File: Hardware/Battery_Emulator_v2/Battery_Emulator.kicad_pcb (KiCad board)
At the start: 2 copper layers, 34.6 x 90.6 mm, 51 parts, among them J1 Vin, J2 USB4105-GF-A-060, J3 Cell1_Vout, Q1 IRFB7545PBF, SW1 Jumper, SW2 Jumper, U1 MCP4651T-103E_ST, U10 ATmega328PB-A, U2 ISO1640BDR, U3 74AHC2G125DP,125, U4 FT230XS-R, U5 KA78M05_TO252, U7 LM317_TO-220, U8 MCP6001UT-I/OT, U9 KA78M05_TO252, Y1 Crystal_GND24

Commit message: Update Battery_Emulator.kicad_pcb
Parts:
- removed RV3, RV4: R_POT, Connector_PinHeader_2.54mm:PinHeader_1x03_P2.54mm_Vertical
- removed SW1, SW2: Jumper, Jumper:SolderJumper-3_P1.3mm_Open_Pad1.0x1.5mm
- added C23: 100n, Capacitor_SMD:C_0805_2012Metric, F.Cu at (192.9, 92.6)
- added C24: 100n, Capacitor_SMD:C_0805_2012Metric, F.Cu at (146.6, 87.4)
- added C25: 10u, Capacitor_SMD:C_0805_2012Metric, F.Cu at (129.4, 87.3)
- added C26: 100n, Capacitor_SMD:C_0805_2012Metric, F.Cu at (192.9, 101.6)
- added C27: 100n, Capacitor_SMD:C_0805_2012Metric, F.Cu at (192.9, 104.6)
- added C28: 10u, Capacitor_SMD:C_0805_2012Metric, F.Cu at (129.0, 92.4)
- added C29: 100n, Capacitor_SMD:C_0805_2012Metric, F.Cu at (146.6, 91.5)
- added C30: 100n, Capacitor_SMD:C_0805_2012Metric, F.Cu at (197.4, 95.6)
- added C31: 100n, Capacitor_SMD:C_0805_2012Metric, F.Cu at (197.4, 98.6)
- added C32: 100n, Capacitor_SMD:C_0805_2012Metric, F.Cu at (145.8, 94.3)
- added C33: 100n, Capacitor_SMD:C_0805_2012Metric, F.Cu at (197.4, 104.6)
- added J4: Cell1_Vout, TerminalBlock_Phoenix:TerminalBlock_Phoenix_MKDS-1,5-2-5.08_1x02_P5.08mm_Horizontal, F.Cu at (155.6, 143.2)
- added JP4: Jumper, Jumper:SolderJumper-3_P1.3mm_Open_Pad1.0x1.5mm_NumberLabels, F.Cu at (190.4, 114.9)
- added JP5: Jumper, Jumper:SolderJumper-3_P1.3mm_Open_Pad1.0x1.5mm_NumberLabels, F.Cu at (150.0, 94.0)
- added JP6: Jumper, Jumper:SolderJumper-3_P1.3mm_Open_Pad1.0x1.5mm_NumberLabels, F.Cu at (150.0, 90.7)
- added PS2: MEE1S1209SC, Converter_DCDC:Converter_DCDC_Murata_MEE1SxxxxSC_THT, F.Cu at (132.0, 85.7)
- added Q2: IRFB7545PBF, Package_TO_SOT_THT:TO-220-3_Horizontal_TabUp, F.Cu at (151.5, 129.6)
- added R10: 0.5m, Resistor_SMD:R_2512_6332Metric, F.Cu at (197.5, 122.1)
- added R8: 780k, Resistor_SMD:R_0805_2012Metric, F.Cu at (154.1, 90.7)
- added R9: 47, Resistor_SMD:R_0805_2012Metric, F.Cu at (201.8, 95.5)
- added U11: ISO1640BDR, Package_SO:SO-8_3.9x4.9mm_P1.27mm, F.Cu at (142.7, 89.4)
- added U12: MCP4651T-103E_ST, Package_SO:TSSOP-14_4.4x5mm_P0.65mm, F.Cu at (197.6, 116.4)
- added U13: KA78M05_TO252, Package_TO_SOT_SMD:TO-252-2, F.Cu at (182.3, 117.1)
- added U14: MCP6001UT-I/OT, Package_TO_SOT_SMD:SOT-23-5, F.Cu at (190.1, 126.0)
- added U6: LM317_TO-220, Package_TO_SOT_THT:TO-220-3_Horizontal_TabUp, F.Cu at (151.6, 114.1)
- R1: value 390k -> 780k
- moved Q1 55.5 mm to (117.6, 134.7)
- moved J3 55.5 mm to (123.5, 143.2)
- moved C1 55.4 mm to (120.0, 106.0)
- moved C11 55.4 mm to (109.2, 66.3)
- moved C12 55.4 mm to (111.2, 83.2)
- moved C15 55.4 mm to (117.6, 91.4)
- moved C16 55.4 mm to (99.9, 92.3)
- moved C17 55.4 mm to (100.1, 87.2)
- moved C18 55.4 mm to (117.6, 87.4)
- moved C2 55.4 mm to (120.0, 102.5)
- moved C21 55.4 mm to (122.6, 68.1)
- moved C22 55.4 mm to (109.2, 62.9)
- moved C3 55.4 mm to (116.6, 121.4)
- moved C4 55.4 mm to (122.7, 56.7)
- moved C5 55.4 mm to (125.4, 60.2)
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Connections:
- C3 pad 1: Net-(SW2-B) -> Net-(U1-P1W)
- U1 pad 6: Net-(SW2-C) -> Net-(U1-P1W)
- U1 pad 9: Net-(SW1-C) -> Net-(U1-P0W)
- U7 pad 1: Net-(SW2-B) -> Net-(U1-P1W)
- U8 pad 3: Net-(SW1-B) -> Net-(U1-P0W)
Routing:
- net Net-(SW2-A): track 36.1 -> 0.00 mm, vias 1 -> 0
- net Net-(U1-P1W): track 0.00 -> 28.3 mm, vias 0 -> 1
- net Net-(SW2-C): track 23.0 -> 0.00 mm, vias 2 -> 0
- net /Cell_1/COUT+: track 76.5 -> 56.0 mm
- net Net-(U8A--): track 25.1 -> 36.6 mm
- net Net-(SW2-B): track 8.80 -> 0.00 mm
- net /Cell_1/GND_ISO: track 18.8 -> 11.4 mm
- net Net-(SW1-B): track 6.42 -> 0.00 mm
- net Net-(SW1-A): track 5.38 -> 0.00 mm
- net Net-(U1-P0B): track 15.3 -> 12.3 mm
- net Net-(SW1-C): track 2.60 -> 0.00 mm
- net +12V: track 30.2 -> 32.8 mm
- net /Cell_2/+5V_ISO: track 0.00 -> 2.09 mm
- net +5V: track 91.9 -> 93.9 mm
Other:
- board size 34.6 x 90.6 mm -> 70 x 96 mm

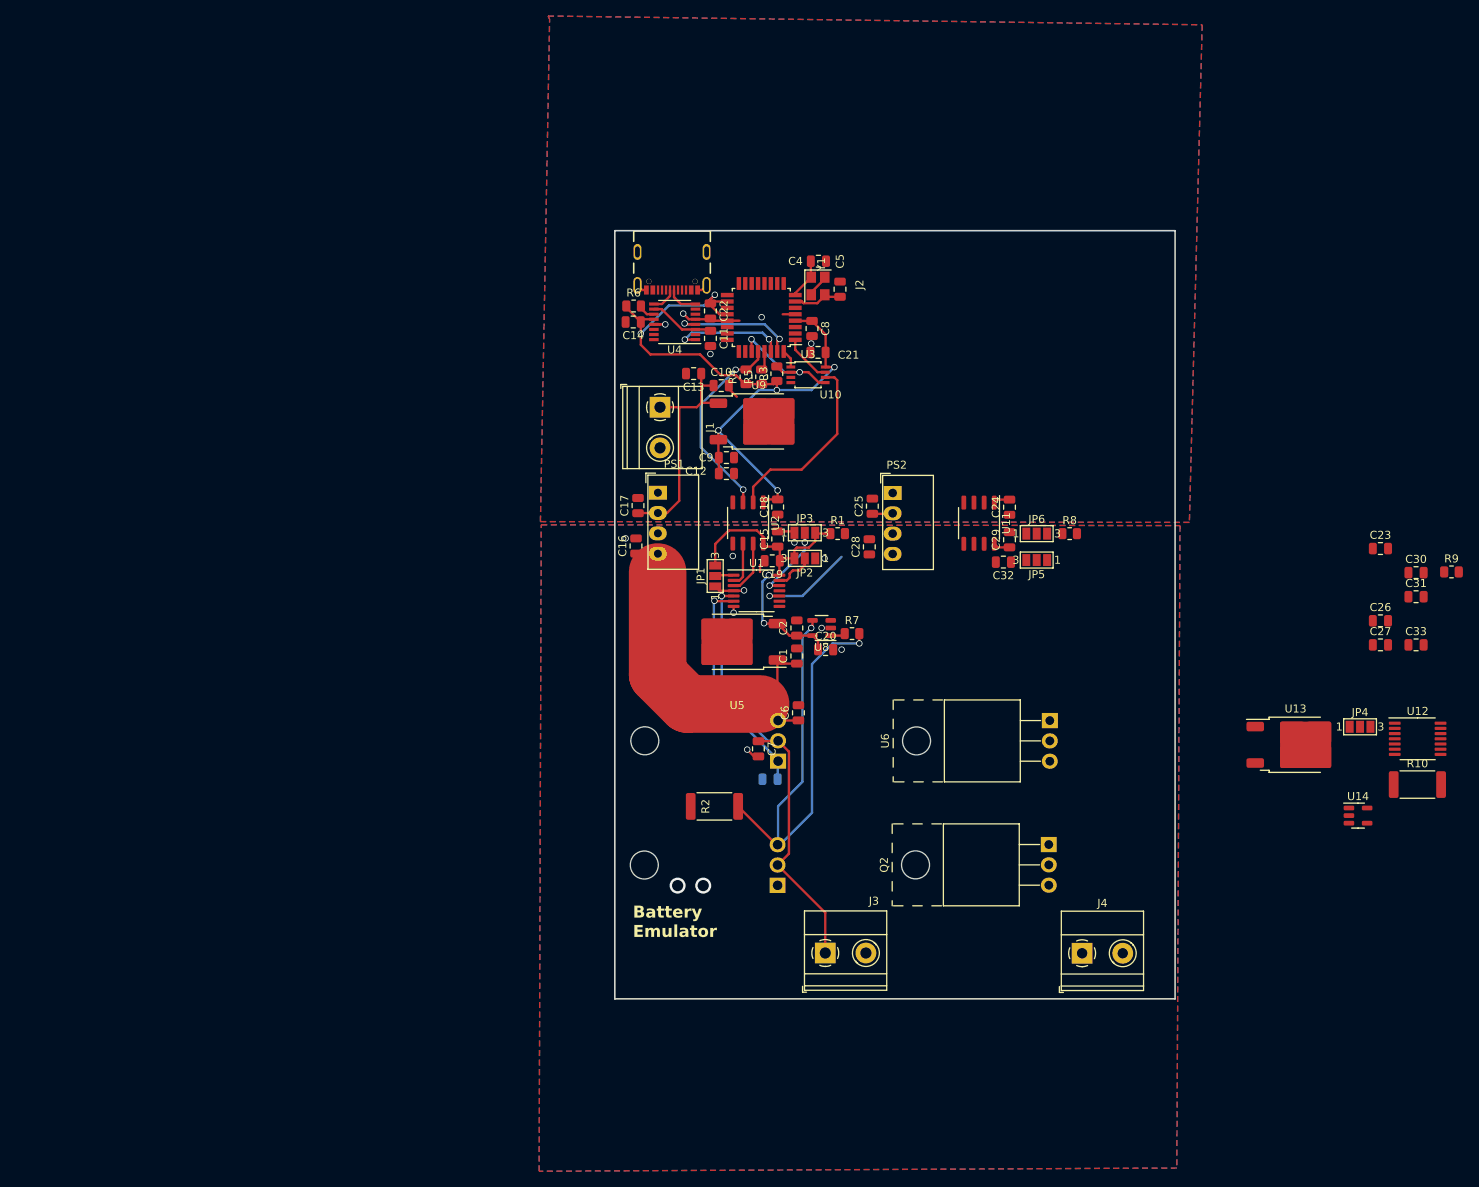
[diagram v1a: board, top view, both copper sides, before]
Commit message: Hardware Update
V2 with four cells with the same layout
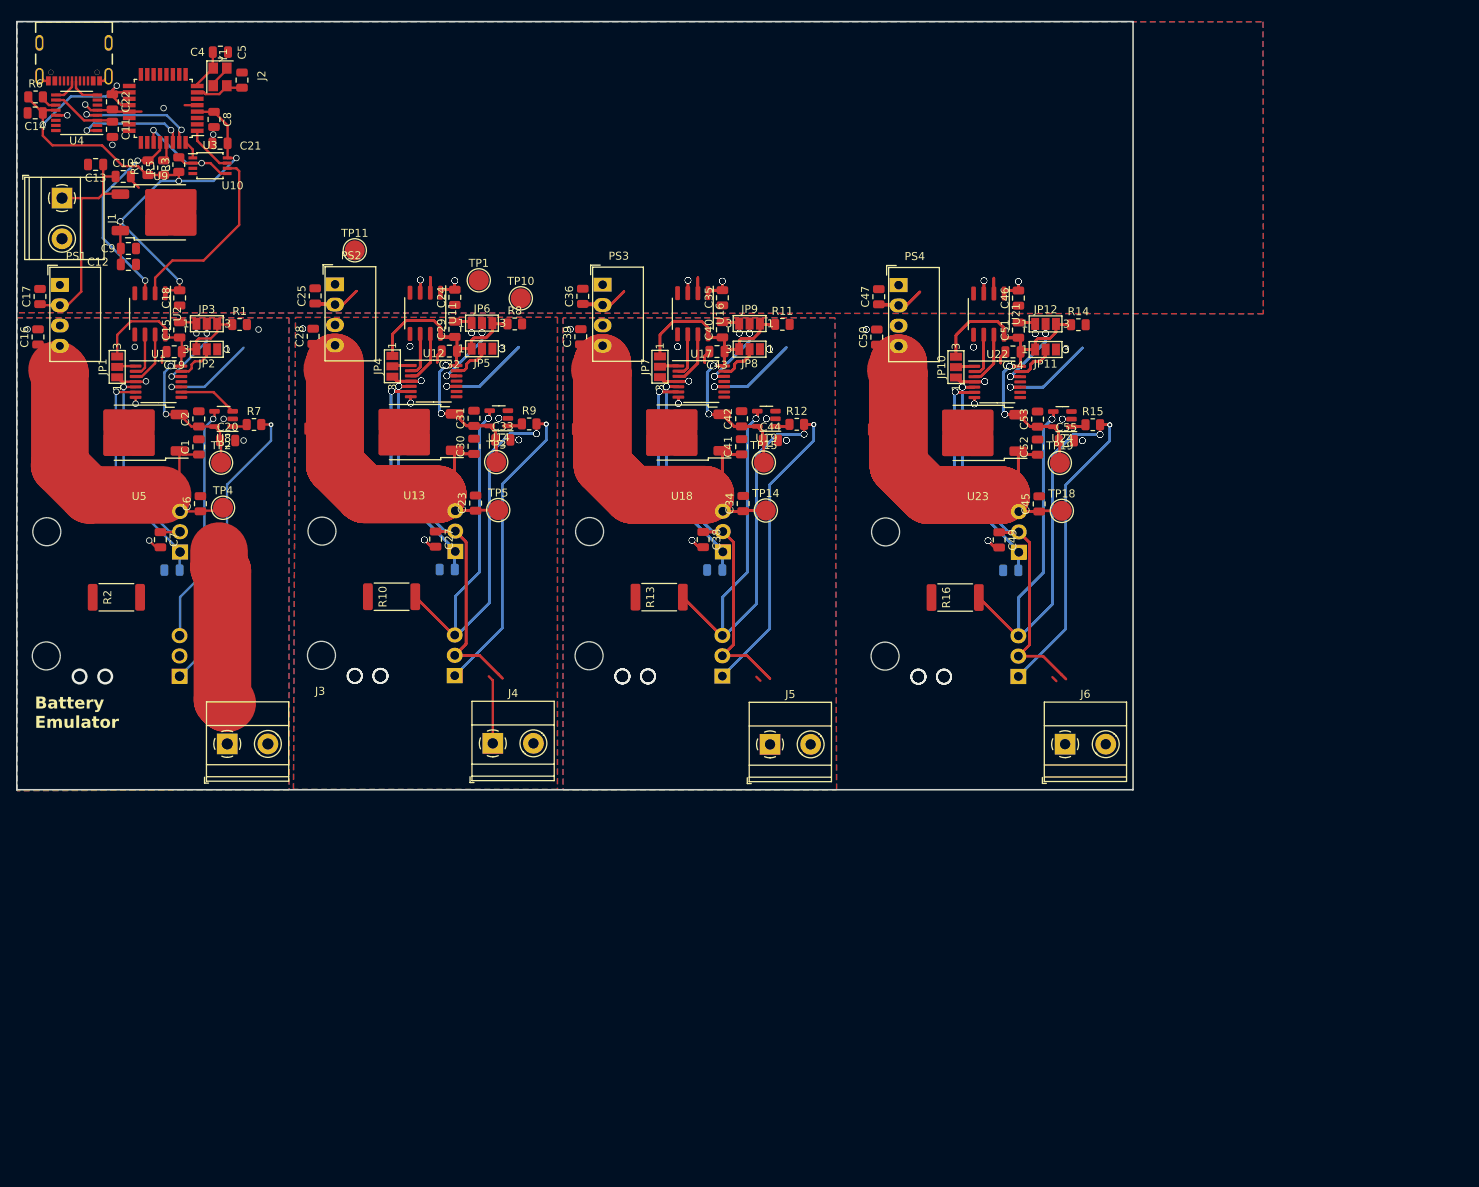
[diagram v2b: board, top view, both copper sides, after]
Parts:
- added C34: 100n, Capacitor_SMD:C_0805_2012Metric, F.Cu at (113.3, 87.0)
- added C35: 100n, Capacitor_SMD:C_0805_2012Metric, F.Cu at (110.7, 61.2)
- added C36: 10u, Capacitor_SMD:C_0805_2012Metric, F.Cu at (93.2, 61.1)
- added C37: 100n, Capacitor_SMD:C_0805_2012Metric, B.Cu at (109.7, 95.3)
- added C38: 100n, Capacitor_SMD:C_0805_2012Metric, F.Cu at (108.3, 91.5)
- added C39: 10u, Capacitor_SMD:C_0805_2012Metric, F.Cu at (93.0, 66.1)
- added C40: 100n, Capacitor_SMD:C_0805_2012Metric, F.Cu at (110.7, 65.2)
- added C41: 100n, Capacitor_SMD:C_0805_2012Metric, F.Cu at (113.1, 79.9)
- added C42: 100n, Capacitor_SMD:C_0805_2012Metric, F.Cu at (113.1, 76.4)
- added C43: 100n, Capacitor_SMD:C_0805_2012Metric, F.Cu at (110.0, 68.0)
- added C44: 100n, Capacitor_SMD:C_0805_2012Metric, F.Cu at (116.7, 79.1)
- added C45: 100n, Capacitor_SMD:C_0805_2012Metric, F.Cu at (150.3, 87.0)
- added C46: 100n, Capacitor_SMD:C_0805_2012Metric, F.Cu at (147.7, 61.3)
- added C47: 10u, Capacitor_SMD:C_0805_2012Metric, F.Cu at (130.2, 61.1)
- added C48: 100n, Capacitor_SMD:C_0805_2012Metric, B.Cu at (146.7, 95.3)
- added C49: 100n, Capacitor_SMD:C_0805_2012Metric, F.Cu at (145.3, 91.5)
- added C50: 10u, Capacitor_SMD:C_0805_2012Metric, F.Cu at (130.0, 66.2)
- added C51: 100n, Capacitor_SMD:C_0805_2012Metric, F.Cu at (147.7, 65.3)
- added C52: 100n, Capacitor_SMD:C_0805_2012Metric, F.Cu at (150.1, 79.9)
- added C53: 100n, Capacitor_SMD:C_0805_2012Metric, F.Cu at (150.1, 76.4)
- added C54: 100n, Capacitor_SMD:C_0805_2012Metric, F.Cu at (147.0, 68.0)
- added C55: 100n, Capacitor_SMD:C_0805_2012Metric, F.Cu at (153.7, 79.1)
- added J5: Cell3_Vout, TerminalBlock_Phoenix:TerminalBlock_Phoenix_MKDS-1,5-2-5.08_1x02_P5.08mm_Horizontal, F.Cu at (116.6, 117.1)
- added J6: Cell4_Vout, TerminalBlock_Phoenix:TerminalBlock_Phoenix_MKDS-1,5-2-5.08_1x02_P5.08mm_Horizontal, F.Cu at (153.5, 117.1)
- added JP10: Jumper, Jumper:SolderJumper-3_P1.3mm_Open_Pad1.0x1.5mm_NumberLabels, F.Cu at (139.9, 69.9)
- added JP11: Jumper, Jumper:SolderJumper-3_P1.3mm_Open_Pad1.0x1.5mm_NumberLabels, F.Cu at (151.1, 67.7)
- added JP12: Jumper, Jumper:SolderJumper-3_P1.3mm_Open_Pad1.0x1.5mm_NumberLabels, F.Cu at (151.1, 64.5)
- added JP7: Jumper, Jumper:SolderJumper-3_P1.3mm_Open_Pad1.0x1.5mm_NumberLabels, F.Cu at (102.9, 69.9)
- added JP8: Jumper, Jumper:SolderJumper-3_P1.3mm_Open_Pad1.0x1.5mm_NumberLabels, F.Cu at (114.1, 67.7)
- added JP9: Jumper, Jumper:SolderJumper-3_P1.3mm_Open_Pad1.0x1.5mm_NumberLabels, F.Cu at (114.1, 64.5)
- added PS3: MEE1S1209SC, Converter_DCDC:Converter_DCDC_Murata_MEE1SxxxxSC_THT, F.Cu at (95.7, 59.6)
- added PS4: MEE1S1209SC, Converter_DCDC:Converter_DCDC_Murata_MEE1SxxxxSC_THT, F.Cu at (132.7, 59.7)
- added Q3: IRFB7545PBF, Package_TO_SOT_THT:TO-220-3_Horizontal_TabUp, B.Cu at (110.7, 108.5)
- added Q4: IRFB7545PBF, Package_TO_SOT_THT:TO-220-3_Horizontal_TabUp, B.Cu at (147.7, 108.6)
- added R11: 780k, Resistor_SMD:R_0805_2012Metric, F.Cu at (118.2, 64.6)
- added R12: 47, Resistor_SMD:R_0805_2012Metric, F.Cu at (120.0, 77.1)
- added R13: 0.5m, Resistor_SMD:R_2512_6332Metric, F.Cu at (102.8, 98.7)
- added R14: 780k, Resistor_SMD:R_0805_2012Metric, F.Cu at (155.2, 64.6)
- added R15: 47, Resistor_SMD:R_0805_2012Metric, F.Cu at (157.0, 77.1)
- added R16: 0.5m, Resistor_SMD:R_2512_6332Metric, F.Cu at (139.8, 98.7)
- added TP1: 5V, TestPoint:TestPoint_Pad_D2.5mm, F.Cu at (80.2, 59.1)
- added TP10: GND, TestPoint:TestPoint_Pad_D2.5mm, F.Cu at (85.5, 61.3)
- added TP11: 12V, TestPoint:TestPoint_Pad_D2.5mm, F.Cu at (64.7, 55.3)
- added TP14: 9V_ISO, TestPoint:TestPoint_Pad_D2.5mm, F.Cu at (116.1, 87.8)
- added TP15: 5V_ISO, TestPoint:TestPoint_Pad_D2.5mm, F.Cu at (115.8, 81.8)
- added TP18: 9V_ISO, TestPoint:TestPoint_Pad_D2.5mm, F.Cu at (153.1, 87.9)
- added TP19: 5V_ISO, TestPoint:TestPoint_Pad_D2.5mm, F.Cu at (152.8, 81.9)
- added TP2: 5V_ISO, TestPoint:TestPoint_Pad_D2.5mm, F.Cu at (48.0, 81.9)
- added TP3: 5V_ISO, TestPoint:TestPoint_Pad_D2.5mm, F.Cu at (82.4, 81.8)
- added TP4: 9V_ISO, TestPoint:TestPoint_Pad_D2.5mm, F.Cu at (48.2, 87.5)
- added TP5: 9V_ISO, TestPoint:TestPoint_Pad_D2.5mm, F.Cu at (82.6, 87.8)
- added U15: LM317_TO-220, Package_TO_SOT_THT:TO-220-3_Horizontal_TabUp, B.Cu at (110.7, 93.0)
- added U16: ISO1640BDR, Package_SO:SO-8_3.9x4.9mm_P1.27mm, F.Cu at (107.0, 63.2)
- added U17: MCP4651T-103E_ST, Package_SO:TSSOP-14_4.4x5mm_P0.65mm, F.Cu at (108.0, 71.7)
- added U18: KA78M05_TO252, Package_TO_SOT_SMD:TO-252-2, F.Cu at (105.6, 78.1)
- added U19: MCP6001UT-I/OT, Package_TO_SOT_SMD:SOT-23-5, F.Cu at (116.2, 76.4)
- added U20: LM317_TO-220, Package_TO_SOT_THT:TO-220-3_Horizontal_TabUp, B.Cu at (147.7, 93.1)
- added U21: ISO1640BDR, Package_SO:SO-8_3.9x4.9mm_P1.27mm, F.Cu at (144.0, 63.3)
- added U22: MCP4651T-103E_ST, Package_SO:TSSOP-14_4.4x5mm_P0.65mm, F.Cu at (145.0, 71.8)
- added U23: KA78M05_TO252, Package_TO_SOT_SMD:TO-252-2, F.Cu at (142.6, 78.1)
- added U24: MCP6001UT-I/OT, Package_TO_SOT_SMD:SOT-23-5, F.Cu at (153.2, 76.4)
- C26, Q2, U6: moved to B.Cu
- J4: value Cell1_Vout -> Cell2_Vout
- moved U12 130.9 mm to (74.6, 71.7)
- moved R10 130.4 mm to (69.3, 98.6), turned to 180 degrees
- moved JP4 129.1 mm to (69.4, 69.8), turned to 90 degrees
- moved C31 119.9 mm to (79.6, 76.3), turned to 90 degrees
- moved C27 118.8 mm to (74.8, 91.4), turned to -90 degrees
- moved C30 118.8 mm to (79.6, 79.8), turned to 90 degrees
- moved U14 118.3 mm to (82.7, 76.3), turned to 180 degrees
- moved C33 117.0 mm to (83.2, 79.0)
- moved U13 116.9 mm to (72.2, 78.0), turned to 180 degrees
- moved C26 116.8 mm to (76.3, 95.2), turned to 180 degrees
- moved R9 116.8 mm to (86.5, 77.0)
- moved C23 113.3 mm to (79.8, 86.9), turned to 90 degrees
- moved C21 79.2 mm to (47.9, 41.9)
- moved C22 79.2 mm to (34.4, 36.8)
- moved C3 79.2 mm to (41.9, 95.3)
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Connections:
- C17 pad 2: GND -> Net-(PS1--Vin)
- C25 pad 2: GND -> Net-(PS2--Vin)
- C7 pad 1: /Cell_1/COUT+ -> Net-(U8A--)
- J3 pad 1: /Cell_1/COUT+ -> Net-(U8A--)
- PS1 pad 1: GND -> Net-(PS1--Vin)
- PS2 pad 1: GND -> Net-(PS2--Vin)
- Q1 pad 2: /Cell_1/COUT+ -> Net-(U8A--)
- U1 pad 5: /Cell_1/COUT+ -> Net-(U8A--)
- U7 pad 2: /Cell_1/COUT+ -> Net-(U8A--)
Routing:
- net Net-(U24A--): track 0.00 -> 173.1 mm, vias 0 -> 5
- net Net-(U14A--): track 0.00 -> 173.1 mm, vias 0 -> 5
- net Net-(U19A--): track 0.00 -> 173.1 mm, vias 0 -> 5
- net /Cell_2/COUT+: track 0.00 -> 151.3 mm, vias 0 -> 3
- net /Cell_3/COUT+: track 0.00 -> 143.4 mm, vias 0 -> 3
- net /Cell_4/COUT+: track 0.00 -> 143.4 mm, vias 0 -> 3
- net /Cell_4/+9V_ISO: track 0.00 -> 140.4 mm
- net /Cell_2/+9V_ISO: track 0.00 -> 140.4 mm
- net /Cell_3/+9V_ISO: track 0.00 -> 140.4 mm
- net /Cell_4/+5V_ISO: track 0.00 -> 132.4 mm, vias 0 -> 6
- net /Cell_3/+5V_ISO: track 0.00 -> 132.4 mm, vias 0 -> 6
- net /Cell_2/+5V_ISO: track 2.09 -> 132.4 mm, vias 0 -> 6
- net Net-(Q3-Pad1): track 0.00 -> 107.6 mm, vias 0 -> 3
- net Net-(Q2-Pad1): track 0.00 -> 107.6 mm, vias 0 -> 3
- net Net-(Q4-Pad1): track 0.00 -> 107.6 mm, vias 0 -> 3
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- added copper zone on B.Cu, net /Cell_2/GND_ISO
- added copper zone on F.Cu, net /Cell_2/GND_ISO
- added copper zone on B.Cu, net /Cell_3/GND_ISO
- added copper zone on F.Cu, net /Cell_3/GND_ISO
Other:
- board size 70 x 96 mm -> 139.5 x 96 mm
